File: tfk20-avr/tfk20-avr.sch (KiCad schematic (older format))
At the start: 29 parts, among them J101 USB_C_Receptacle_USB2.0, SW101 Reset, U101 ATmega32U4-AU, Y101 16MHz

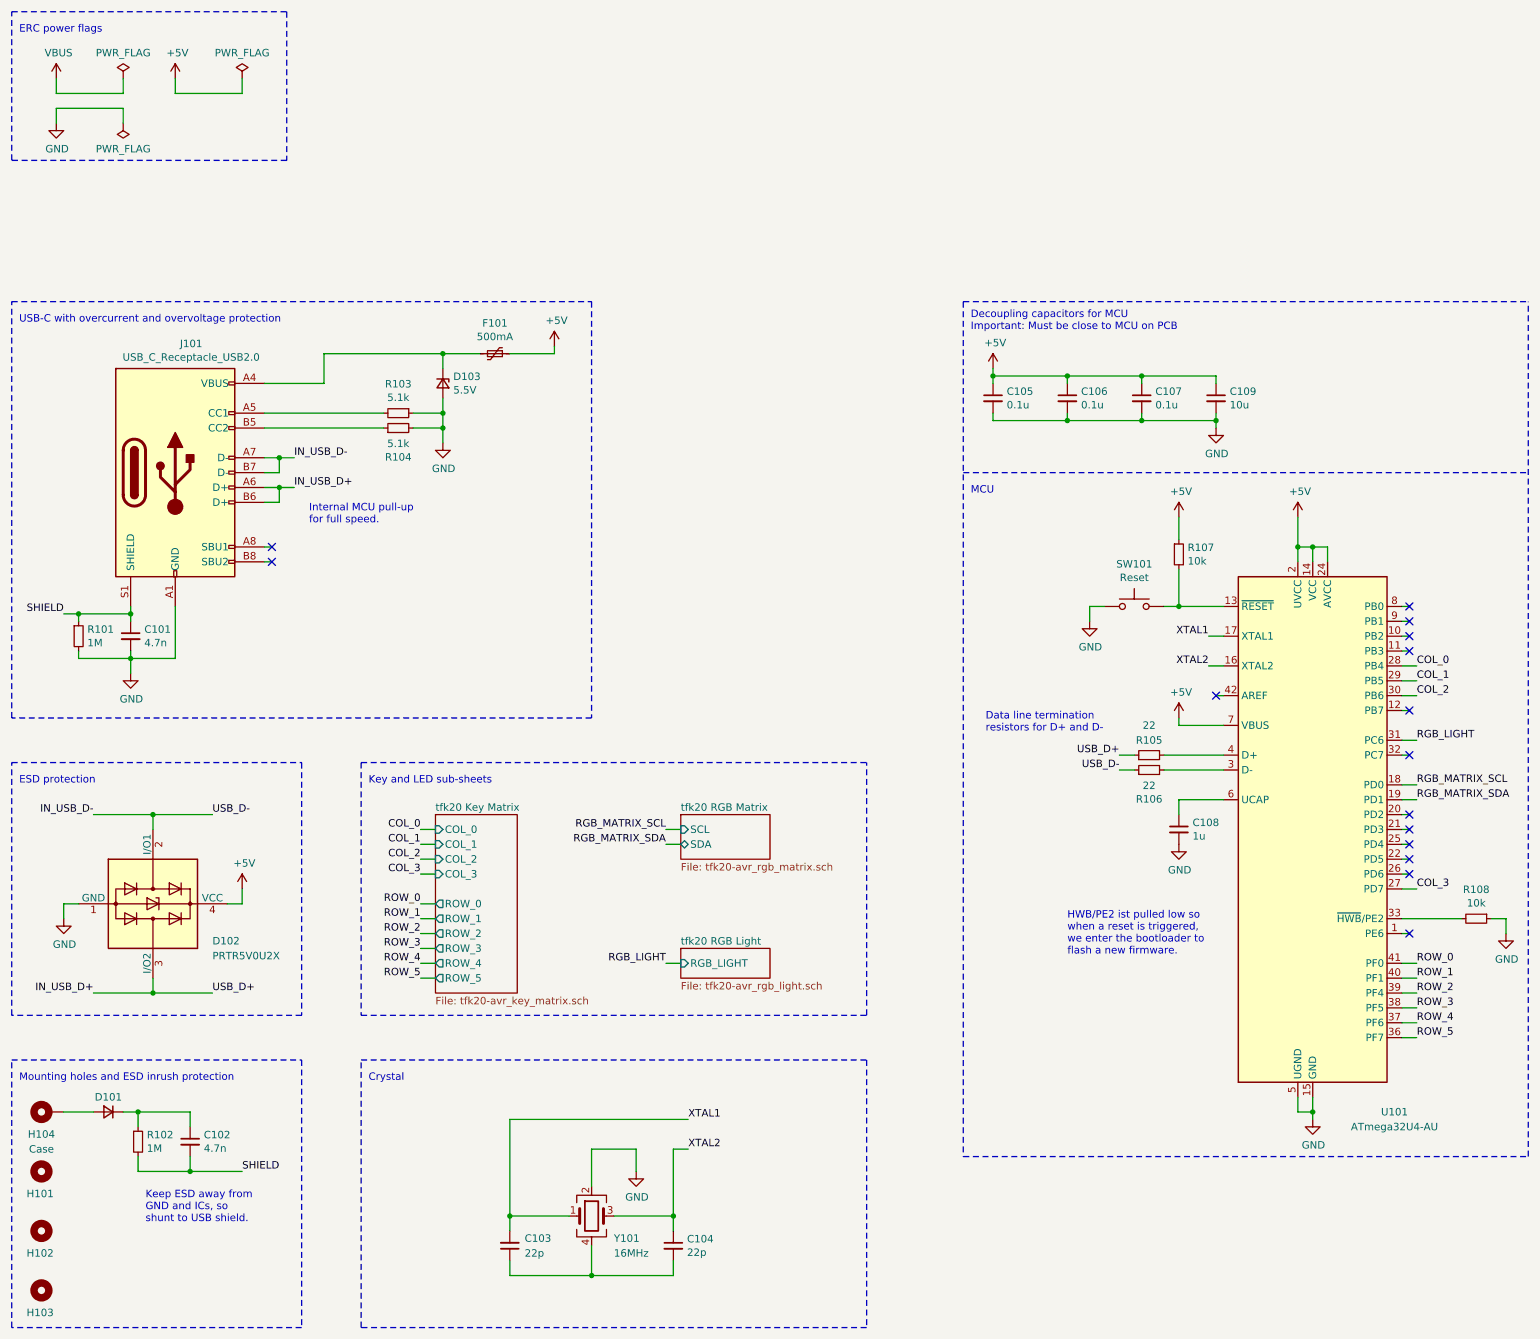
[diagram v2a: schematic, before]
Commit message: Add ISP header
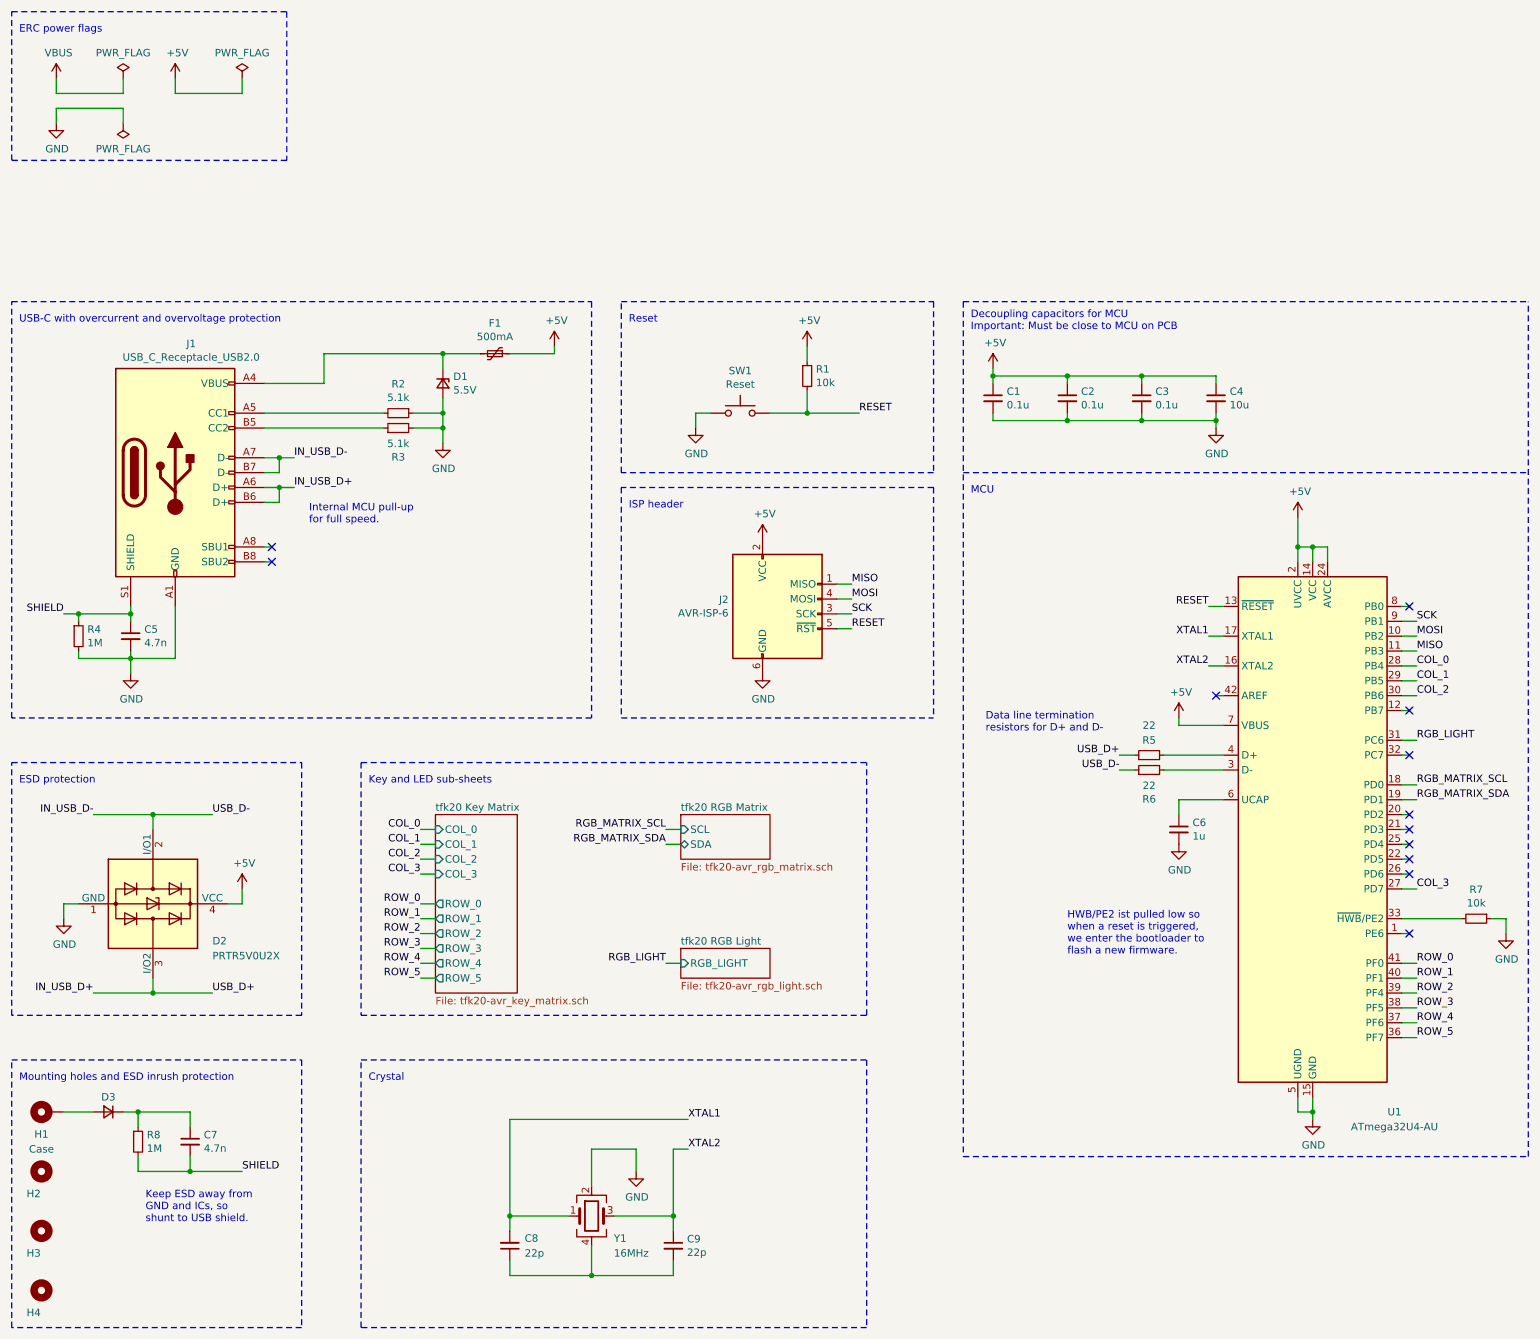
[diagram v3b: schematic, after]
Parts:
- added J2: AVR-ISP-6, symbol Connector:AVR-ISP-6
- renumbered C105 to C1, C106 to C2, C107 to C3, C109 to C4, C101 to C5, C108 to C6, C102 to C7, C103 to C8, C104 to C9, D103 to D1, D102 to D2, D101 to D3, F101 to F1, H104 to H1, H101 to H2, H102 to H3, H103 to H4, J101 to J1, R107 to R1, R103 to R2, R104 to R3, R101 to R4, R105 to R5, R106 to R6, R108 to R7, R102 to R8, SW101 to SW1, U101 to U1, Y101 to Y1
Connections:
- net +5V: now also J2.2 (VCC)
- net GND: now also J2.6 (GND)
- net MOSI: now reaches U1.10 (PB2)
- net MOSI: now also J2.4 (MOSI)
- net MISO: now reaches U1.11 (PB3)
- net MISO: now also J2.1 (MISO)
- net RESET: now reaches R1.2, SW1.2, U1.13 (~RESET)
- net RESET: now also J2.5 (~RST)
- net SCK: now reaches U1.9 (PB1)
- net SCK: now also J2.3 (SCK)
- no-connect marks 15 -> 12
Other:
- note added: "ISP header"
- note added: "Reset"
- moved on the sheet: R1, SW1
